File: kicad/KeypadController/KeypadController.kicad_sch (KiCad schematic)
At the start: 18 parts, among them J1 ISP, J2 Keypad, J3 Switch, J4 Cable, U1 MAX232, U2 ATmega48-20P

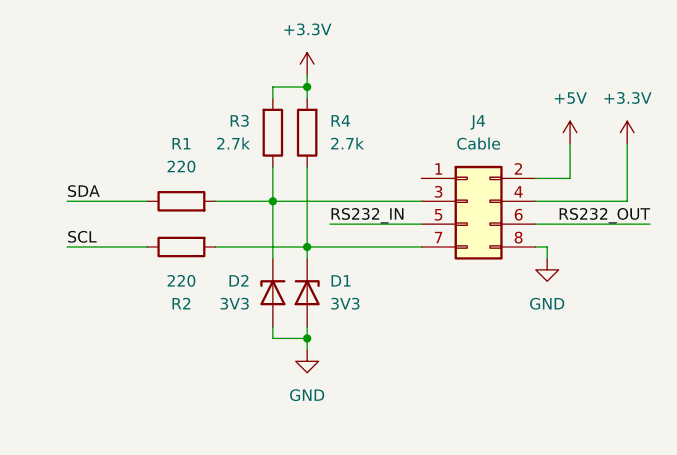
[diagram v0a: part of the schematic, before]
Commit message: Fixed keypad wiring schematics
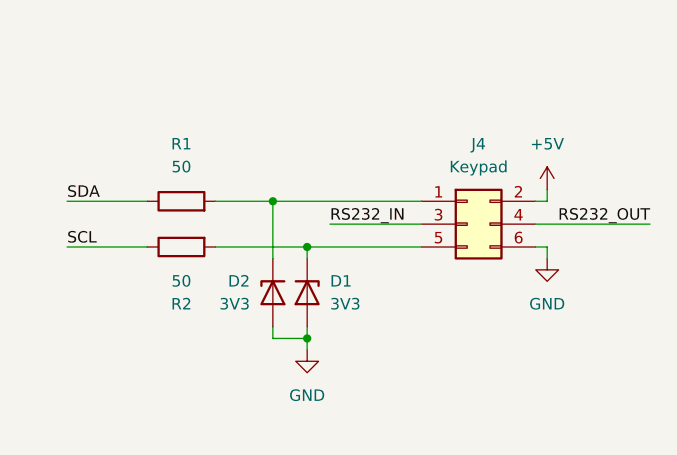
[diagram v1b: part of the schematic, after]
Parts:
- removed J4: Cable, symbol Connector_Generic:Conn_02x04_Odd_Even
- removed R3, R4: 2.7k, Resistor_THT:R_Axial_DIN0204_L3.6mm_D1.6mm_P2.54mm_Vertical, symbol Device:R
- added J4: Keypad, symbol Connector_Generic:Conn_02x03_Odd_Even
- R1, R2: value 220 -> 50
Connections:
- net +5V: now also J4.2 (Pin_2)
- net GND: now also J4.6 (Pin_6)
- net RS232_IN: now also J4.3 (Pin_3)
- net RS232_OUT: now also J4.4 (Pin_4)
- net at D1.1 (K), R2.2: now also J4.5 (Pin_5)
- net at D2.1 (K), R1.2: now also J4.1 (Pin_1)
